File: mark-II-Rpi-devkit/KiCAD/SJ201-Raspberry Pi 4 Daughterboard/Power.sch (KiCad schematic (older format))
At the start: 23 parts, among them J1 Barrel_Jack, J5 PowerTP, Q3 AO3415A, U1 XL4015, U4 AZ1117CH-3.3

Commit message: Update BOM - fix OPL numbers for Seeed PCBA
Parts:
- C1: SKU (none) -> (none)
- C6, C8: SKU (none) -> 508000001
- C60: MPN CL10A226MQ8NRNC -> CL10A226MQ8NRNE
- PWR1: Link (none) -> https://lcsc.com/product-detail/Others_TOGIALED-TJ-S1608SW6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; MPN TJ-S1608SW6TGLC2R-A5 -> 19-217-R6C-AL1M2VY-3T; SKU (none) -> 304090042
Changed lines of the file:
@@
 F 4 "VZH221M1HTR-1010" H 1680 4750 20  0001 C CNN "MPN"
 F 5 "C134819" H 1650 4600 50  0001 C CNN "LCSC"
+F 6 " " H 1650 4600 50  0001 C CNN "SKU"
 	1    1650 4600
 	1    0    0    -1
@@
 F 4 "RVT1E331M0810" H 4930 4900 20  0001 C CNN "MPN"
 F 5 "C74593" H 4900 4750 50  0001 C CNN "LCSC"
+F 6 "508000001" H 4900 4750 50  0001 C CNN "SKU"
 	1    4900 4750
 	0    1    1    0
@@
 F 4 "GRM155R71A333KA01D" H 5905 4700 20  0001 C CNN "MPN"
 F 5 "C113048" H 5875 4550 50  0001 C CNN "LCSC"
+F 6 "508000001" H 5875 4550 50  0001 C CNN "SKU"
 	1    5875 4550
 	0    1    1    0
@@
 F 2 "Capacitor_SMD:C_0603_1608Metric" H 4125 6225 50  0001 C CNN
 F 3 "" H 4125 6225 50  0001 C CNN
-F 4 "CL10A226MQ8NRNC" H 4125 6225 50  0001 C CNN "MPN"
+F 4 "CL10A226MQ8NRNE" H 4125 6225 50  0001 C CNN "MPN"
 	1    4125 6225
 	1    0    0    -1
@@
 F 2 "LED_SMD:LED_0603_1608Metric" H 6700 4750 50  0001 C CNN
 F 3 "https://datasheet.lcsc.com/szlcsc/1811141223_TOGIALED-TJ-S1608SW6TGLC2R-A5_C192315.pdf" H 6700 4750 50  0001 C CNN
-F 4 "TJ-S1608SW6TGLC2R-A5" H 6700 4750 50  0001 C CNN "MPN"
+F 4 "19-217-R6C-AL1M2VY-3T" H 6700 4750 50  0001 C CNN "MPN"
 F 5 "C192315" H 6700 4750 50  0001 C CNN "LCSC"
+F 6 "https://lcsc.com/product-detail/Others_TOGIALED-TJ-S1608SW6TGLC2R-A5_C192315.html" V 6700 4750 50  0001 C CNN "Link"
+F 7 "304090042" H 6700 4750 50  0001 C CNN "SKU"
 	1    6700 4750
 	0    -1   -1   0

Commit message: Updated KiCAD files to 0.63 for PCB printing & Assembly at JLCPCB
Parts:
- added C37: 22UF, Capacitor_SMD:C_0603_1608Metric, symbol Device:C_Small
- added C5: 10UF, Capacitor_SMD:C_0402_1005Metric, symbol OPL_Capacitor:CERAMIC-2.2UF-25V-10%-X7R_0805_
- added C7: 10nF, Capacitor_SMD:C_0402_1005Metric, symbol OPL_Capacitor:CERAMIC-2.2UF-25V-10%-X7R_0805_
- added D15: D_Schottky, Diode_SMD:D_SOD-123, symbol Device:D_Schottky
- added L2: 2.2UH ±30% 1.55A, Inductor_SMD:L_1210_3225Metric, symbol OPL_Inductor:SMD-INDUCTOR-2.2UH-20%-1.2A_0805_
- added R2: 100K, Resistor_SMD:R_0402_1005Metric, symbol Device:R_Small
- added R3: 75k, Resistor_SMD:R_0402_1005Metric, symbol Device:R_Small
- added R4: 330K, Resistor_SMD:R_0402_1005Metric, symbol Device:R_Small
- added U7: MP2359, Package_TO_SOT_SMD:TSOT-23-6, symbol user:MP2359
- C1: LCSC C134819 -> C134819-DNP
- C2, C3, C4: LCSC (none) -> C52923
- C59: LCSC (none) -> C15525
- C6: footprint user:CP_Elec_8x10.5_OPL -> Capacitor_SMD:CP_Elec_8x10.5; symbol OPL_Capacitor:DIP-ALUMINUM-47UF-16V_D5-H7MM_ -> Device:CP; LCSC C74593 -> C74593-DNP
- C60: LCSC (none) -> C59461
- C63: LCSC (none) -> C1525
- C64: footprint user:CP_Elec_8x10.5_OPL -> Capacitor_SMD:CP_Elec_8x10.5; symbol OPL_Capacitor:DIP-ALUMINUM-47UF-16V_D5-H7MM_ -> Device:CP; LCSC (none) -> C176671
- C8: LCSC C113048 -> C1585
- D14: LCSC (none) -> C22452
- FB8: footprint Resistor_SMD:R_0805_2012Metric -> Resistor_SMD:R_1206_3216Metric; LCSC (none) -> C29107; MPN MPZ2012S101AT000 -> MLB3216-301P3A(f)
- PWR1: LCSC C192315 -> C2286
- Q3: LCSC (none) -> C133233
- R1: LCSC (none) -> C25744
- R27: LCSC (none) -> C25741
- R28: LCSC (none) -> C25104
- R8: LCSC (none) -> C25890
- U1: value XL4015 -> XL4501E1; LCSC C51661 -> C73025; MPN XL4015E1 -> XL4501E1
- U4: LCSC (none) -> C92102
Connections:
- net +12V: now also C64.1; no longer C64.+
- net +5V: now also C6.1, C5.2, R2.1, U7.5 (VIN); no longer C6.+
- net GND: now also C6.2, C64.2, C37.2, C5.1, D15.2 (A), R4.1, U7.2 (GND); no longer C6.-, C64.-
- net +1V0: now reaches J5.4 (Pin_4)
- net +1V0: now also C37.1, L2.2, R3.1
- new net: R3.2, R4.2, U7.3 (FB)
- new net: C7.1, D15.1 (K), L2.1, U7.6 (SW)
- new net: C7.2, U7.1 (BST)
- new net: R2.2, U7.4 (EN)
- no-connect marks 1 -> 0
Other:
- note added: "1.0v Buck for XMOS"
- note added: "Power Test Points"
- note added: "VFB = 0.6V\nVO = 0.6 x (1 + 30/47) = 0.98V\n"
- moved on the sheet: C59, C60, U4

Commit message: Change USB IC to CM108B, add in Line Out jack, prep for 2 PCB sandwich
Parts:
- C64: LCSC C176671 -> C176671-DNP
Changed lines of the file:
@@
 Sheet 2 6
 Title "Power"
-Date "2020-07-22"
-Rev "0.63"
+Date "2020-07-23"
+Rev "0.64"
 Comp "Mycroft"
 Comment1 "Power Converter"
@@
 F 4 "SMD CAP Aluminum 470uF-16V;D8.0*H10.2mm" H 6255 2875 20  0001 C CNN "MPN"
 F 5 "302030006" H 6255 2875 20  0001 C CNN "SKU"
-F 6 "C176671" H 6225 2725 50  0001 C CNN "LCSC"
+F 6 "C176671-DNP" H 6225 2725 50  0001 C CNN "LCSC"
 	1    6225 2725
 	1    0    0    -1

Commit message: Change vertical barrel connector, files sent to JLC PCB for printing and assembly.
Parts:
- J1: footprint mycroft:CUI_PJ-090H -> user:BarrelJack_Vertical; Digikey 102-5561-2-ND -> (none); LCSC (none) -> C381117; Link https://www.digikey.com/product-detail/en/cui-devices/PJ-09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 -> https://lcsc.com/product-detail/Power-Connectors_XKB-Connec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; MPN PJ-090H -> DC-012-5A-2.0
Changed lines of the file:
@@
 Sheet 2 6
 Title "Power"
-Date "2020-07-23"
-Rev "0.64"
+Date "2020-07-24"
+Rev "0.65"
 Comp "Mycroft"
 Comment1 "Power Converter"
@@
 F 0 "J1" H 2682 3050 50  0000 C CNN
 F 1 "Barrel_Jack" H 2682 2959 50  0000 C CNN
-F 2 "mycroft:CUI_PJ-090H" H 2675 2685 50  0001 C CNN
-F 3 "https://www.cuidevices.com/product/resource/pj-090h.pdf" H 2675 2685 50  0001 C CNN
-F 4 "PJ-090H" H 2625 2725 50  0001 C CNN "MPN"
-F 5 "102-5561-2-ND" H 2625 2725 50  0001 C CNN "Digikey"
-F 6 "https://www.digikey.com/product-detail/en/cui-devices/PJ-090H/102-5561-1-ND/9830192" H 2625 2725 50  0001 C CNN "Link"
+F 2 "user:BarrelJack_Vertical" H 2675 2685 50  0001 C CNN
+F 3 "https://datasheet.lcsc.com/szlcsc/2002271745_XKB-Connectivity-DC-012-5A-2-0_C381117.pdf" H 2675 2685 50  0001 C CNN
+F 4 "DC-012-5A-2.0" H 2625 2725 50  0001 C CNN "MPN"
+F 5 "https://lcsc.com/product-detail/Power-Connectors_XKB-Connectivity-DC-012-5A-2-0_C381117.html" H 2625 2725 50  0001 C CNN "Link"
+F 6 "C381117" H 2625 2725 50  0001 C CNN "LCSC"
 	1    2625 2725
 	1    0    0    -1

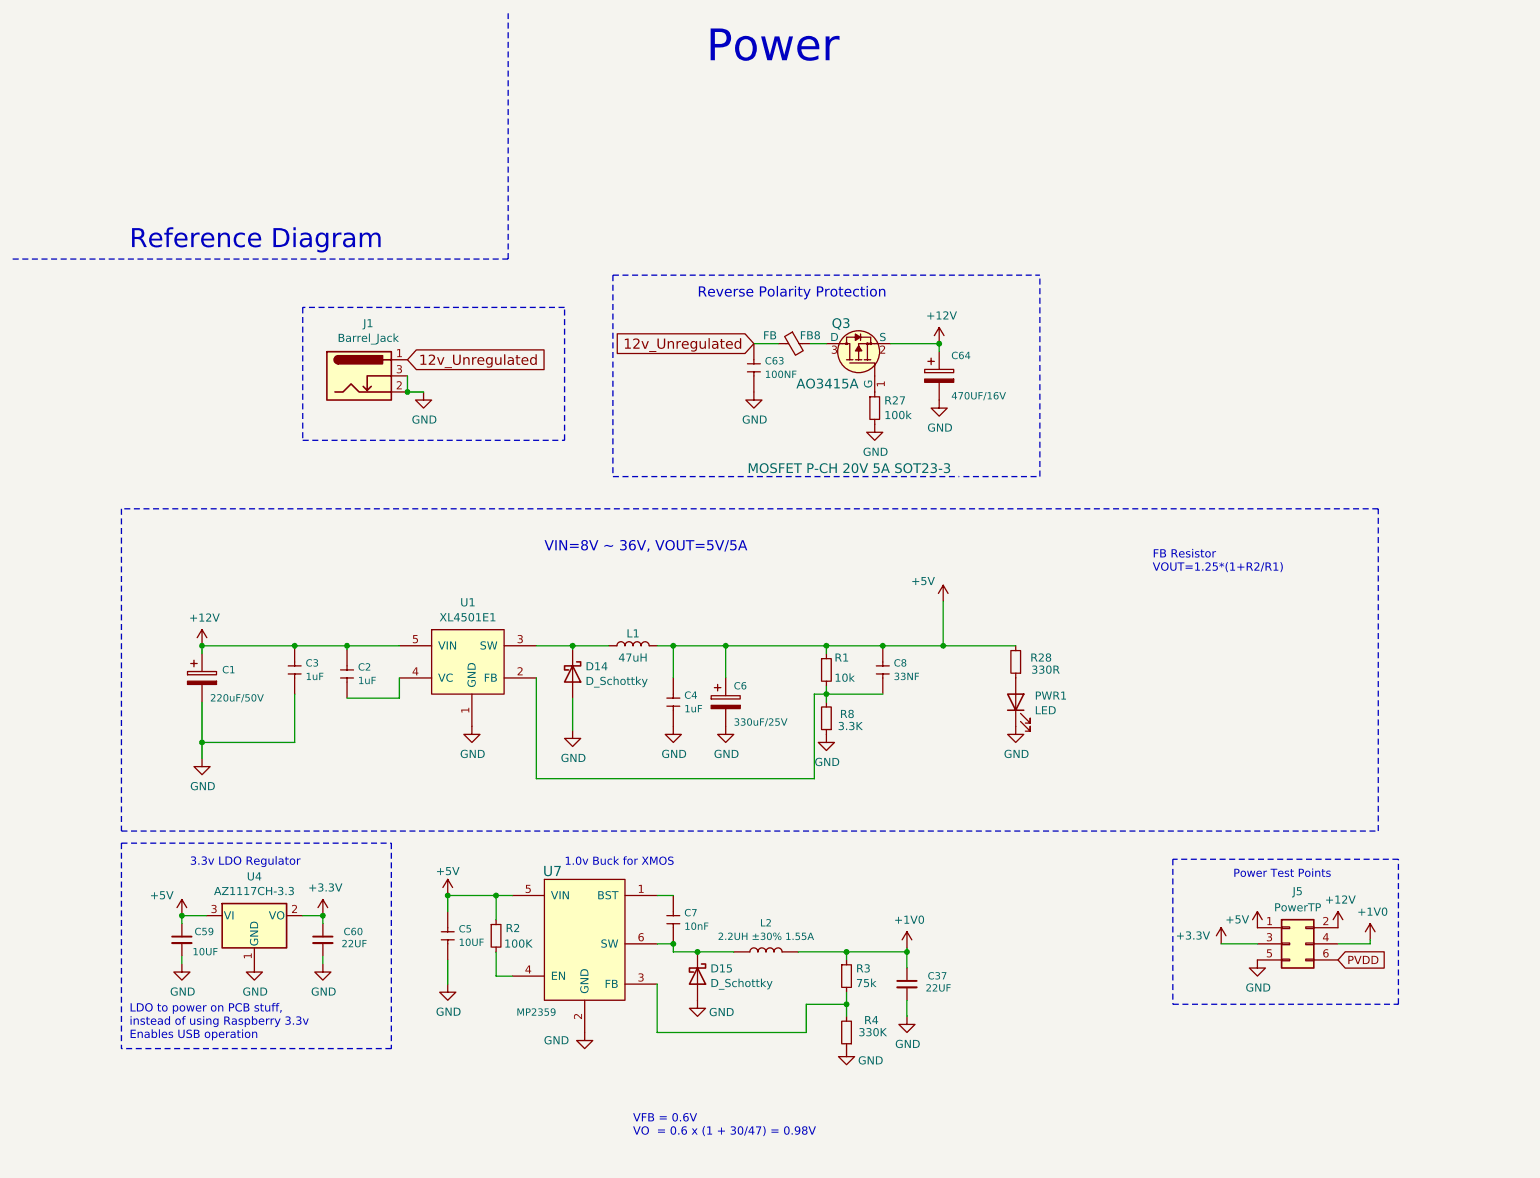
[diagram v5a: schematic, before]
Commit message: Update to v0.66 - printed at JLC - 2nd spin
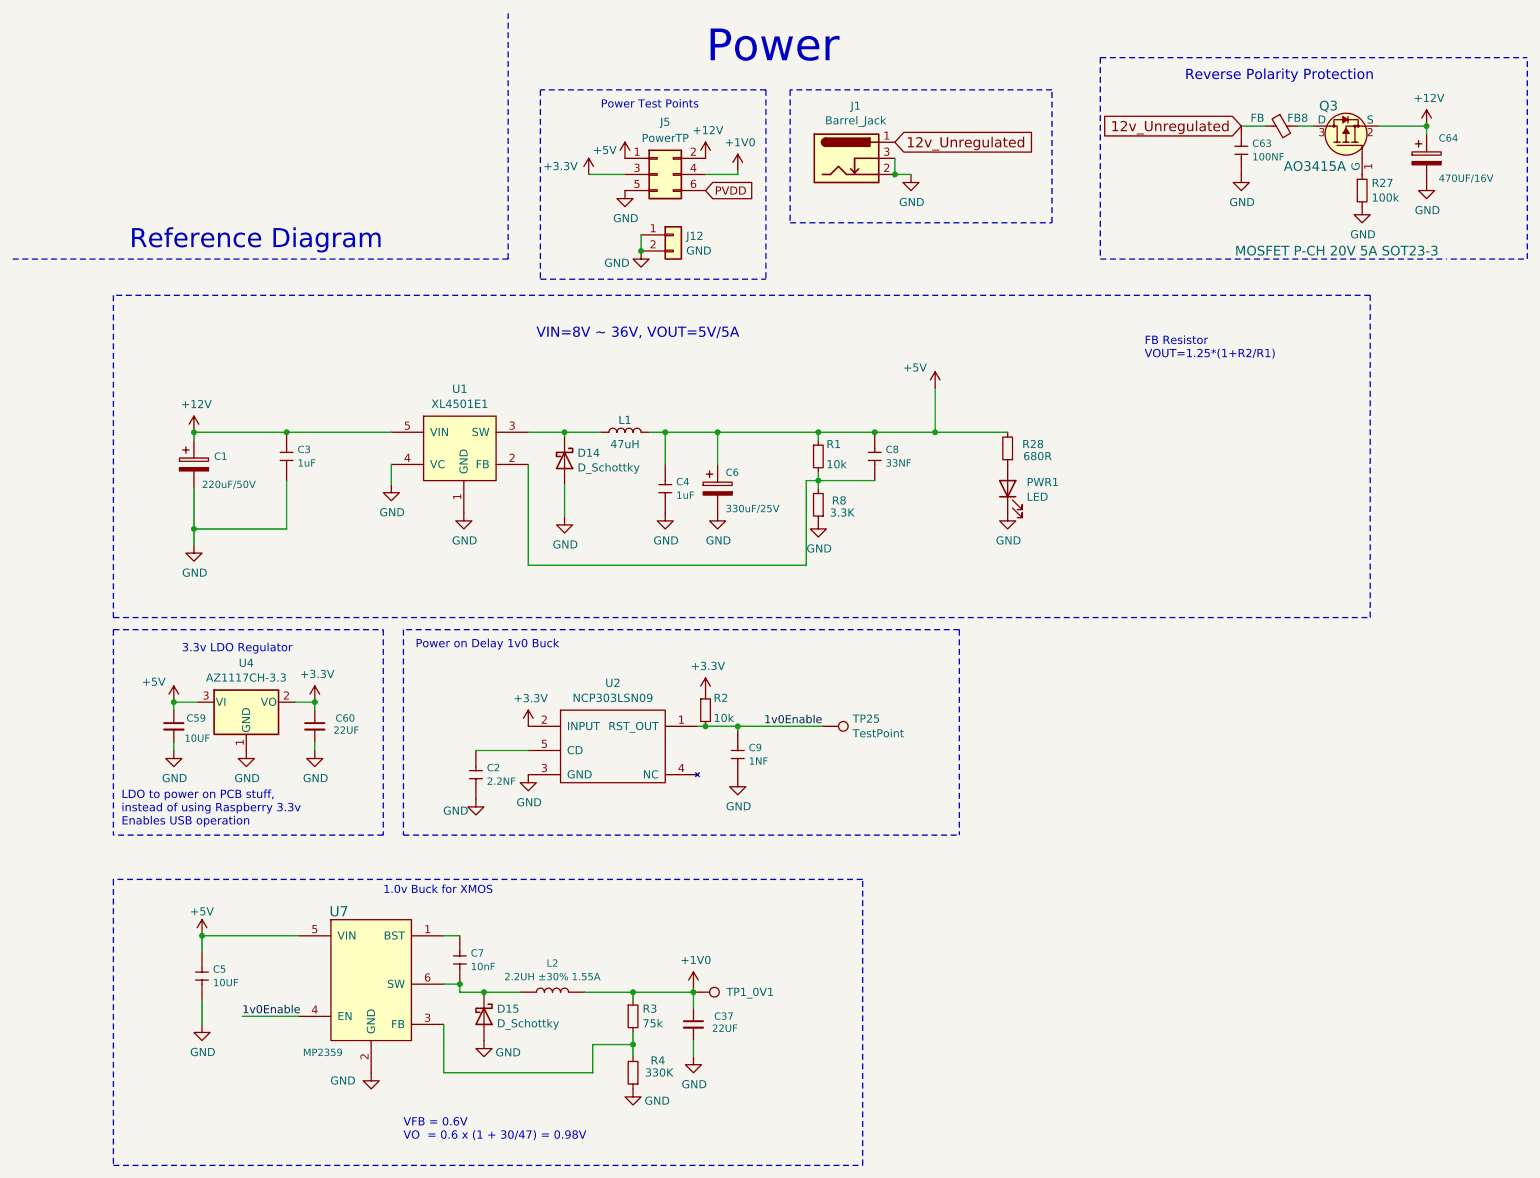
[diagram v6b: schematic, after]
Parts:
- removed C2: 1uF, Capacitor_SMD:C_0402_1005Metric, symbol OPL_Capacitor:CERAMIC-100NF-50V-10%-X7R_0805_
- added C2: 2.2NF, Capacitor_SMD:C_0402_1005Metric, symbol OPL_Capacitor:CERAMIC-2.2UF-25V-10%-X7R_0805_
- added C9: 1NF, Capacitor_SMD:C_0402_1005Metric, symbol OPL_Capacitor:CERAMIC-2.2UF-25V-10%-X7R_0805_
- added J12: GND, Connector_PinHeader_2.54mm:PinHeader_1x02_P2.54mm_Vertical, symbol Connector_Generic:Conn_01x02
- added TP1_0V1, TP25: TestPoint, TestPoint:TestPoint_Pad_D2.0mm, symbol Connector:TestPoint
- added U2: NCP303LSN09, Package_TO_SOT_SMD:SOT-23-5, symbol user:NCP303LSN30
- R2: value 100K -> 10k; LCSC C25741 -> C25744; MPN (none) -> RC0402FR-0710KL
- R28: value 330R -> 680R; Desc (none) -> Chip Resistor - Surface Mount 680Ohms ±1% 1/16W 0402 RoHS; LCSC C25104 -> C25130; MPN RC0402FR-07330RL -> (none); SKU 301010466 -> (none)
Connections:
- net +1V0: now also TP1_0V1.1
- net +3V3: now also R2.1, U2.2 (INPUT)
- net +5V: no longer R2.1
- net GND: now also U1.4 (VC), C2.2, C9.2, J12.1 (Pin_1), J12.2 (Pin_2), U2.3 (GND)
- net 1v0Enable: now reaches R2.2, U7.4 (EN)
- net 1v0Enable: now also C9.1, TP25.1, U2.1 (RST_OUT)
- new net: C2.1, U2.5 (CD)
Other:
- note added: "Power on Delay 1v0 Buck"
- moved on the sheet: C1, C3, C37, C4, C5, C59, C6, C60, C63, C64, C7, C8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
